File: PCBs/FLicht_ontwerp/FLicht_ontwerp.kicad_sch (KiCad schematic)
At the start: 5 parts, among them U1 WeMos_C3_mini, U2 PCF8574

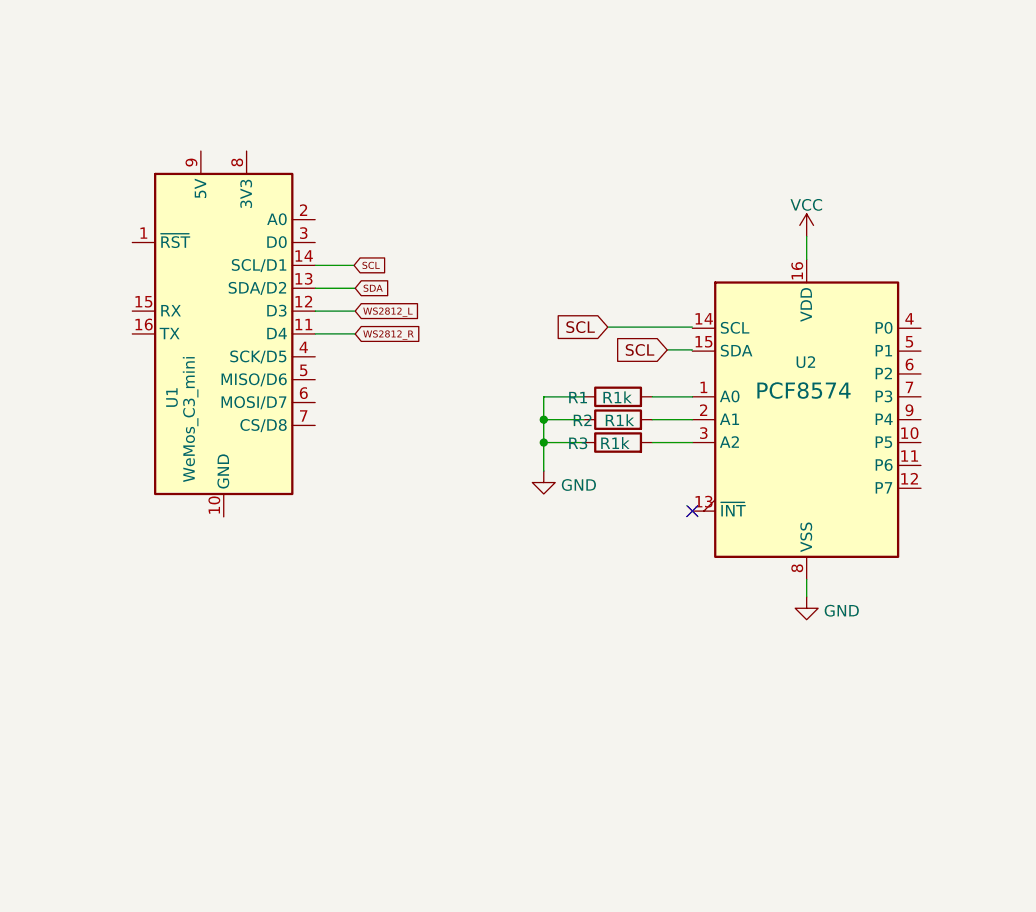
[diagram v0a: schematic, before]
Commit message: SPX3819M5-L IC toegeovegd
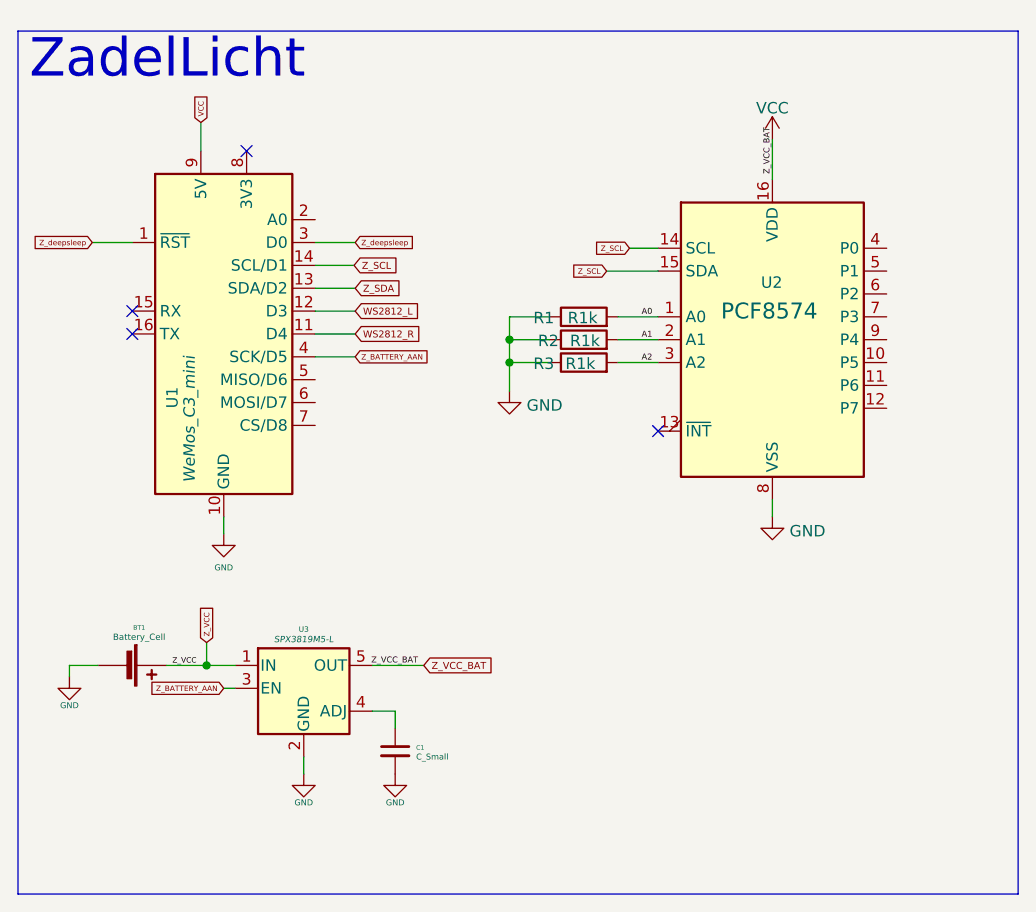
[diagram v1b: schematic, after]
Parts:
- added BT1: Battery_Cell, symbol Device:Battery_Cell
- added C1: C_Small, symbol Device:C_Small
- added U3: SPX3819M5-L, Package_TO_SOT_SMD:SOT-23-5, symbol Regulator_Linear:SPX3819M5-L
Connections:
- net SCL is gone; now on net Z_SCL: U1.14 (SCL/D1)
- net GND1: now also U1.10 (GND)
- net VCC: now also U1.9 (5V), U3.5 (OUT)
- net A0: now reaches R1.2, U2.1 (A0)
- net Z_SCL: now reaches U2.14 (SCL)
- net Z_SCL: now also U2.15 (SDA)
- net A1: now reaches R2.2, U2.2 (A1)
- net A2: now reaches R3.2, U2.3 (A2)
- net Z_deepsleep: now reaches U1.1 (~{RST})
- net Z_deepsleep: now also U1.3 (D0)
- net Z_BATTERY_AAN: now reaches U1.4 (SCK/D5)
- net Z_BATTERY_AAN: now also U3.3 (EN)
- net SDA renamed Z_SDA
- new net: C1.1, U3.4 (ADJ)
- new net GND: BT1.2 (-), C1.2, U3.2 (GND)
- new net Z_VCC: BT1.1 (+), U3.1 (IN)
- no-connect marks 1 -> 4
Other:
- note added: "ZadelLicht"
- moved on the sheet: R1, R2, R3, U2

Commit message: SPX3819M5-L IC toegeovegd
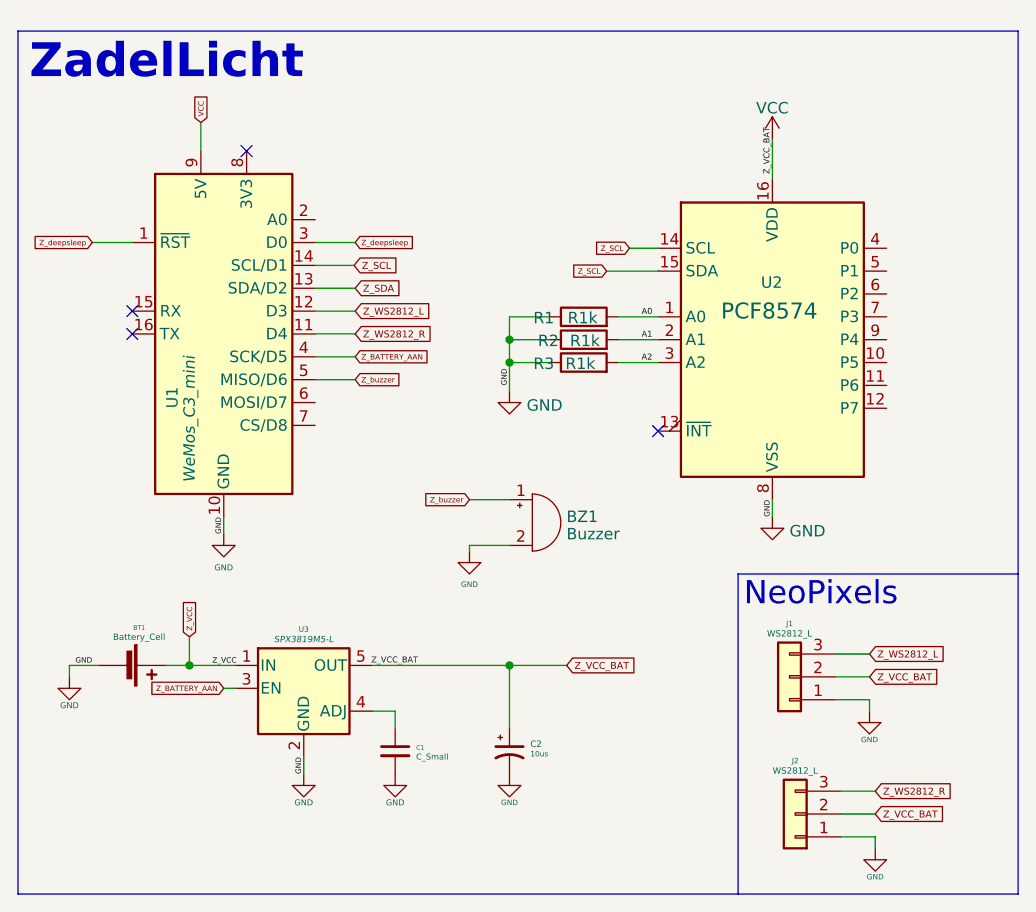
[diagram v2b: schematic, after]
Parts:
- added BZ1: Buzzer, symbol Device:Buzzer
- added C2: 10us, symbol Device:C_Polarized_Small_US
- added J1, J2: WS2812_L, symbol Connector_Generic:Conn_01x03
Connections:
- net GND1 is gone; now on net GND: R1.1, R2.1, R3.1, U1.10 (GND), U2.8 (VSS)
- net GND: now also BZ1.2 (+), C2.2, J1.1 (Pin_1), J2.1 (Pin_1)
- net VCC: now also C2.1, J1.2 (Pin_2), J2.2 (Pin_2)
- net Z_buzzer: now reaches U1.5 (MISO/D6)
- net Z_buzzer: now also BZ1.1 (-)
- net WS2812_L renamed Z_WS2812_L
- net Z_WS2812_L: now also J1.3 (Pin_3)
- net WS2812_R renamed Z_WS2812_R
- net Z_WS2812_R: now also J2.3 (Pin_3)
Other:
- note added: "NeoPixels"
